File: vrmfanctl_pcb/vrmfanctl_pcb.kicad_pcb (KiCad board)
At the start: 2 copper layers, 27.9 x 22.9 mm, 6 parts, among them J1 SATA Power Male, J2 Hole, J3 Pin socket L-shape, J4 Pin socket L-shape, U1 ATtiny85-20PU

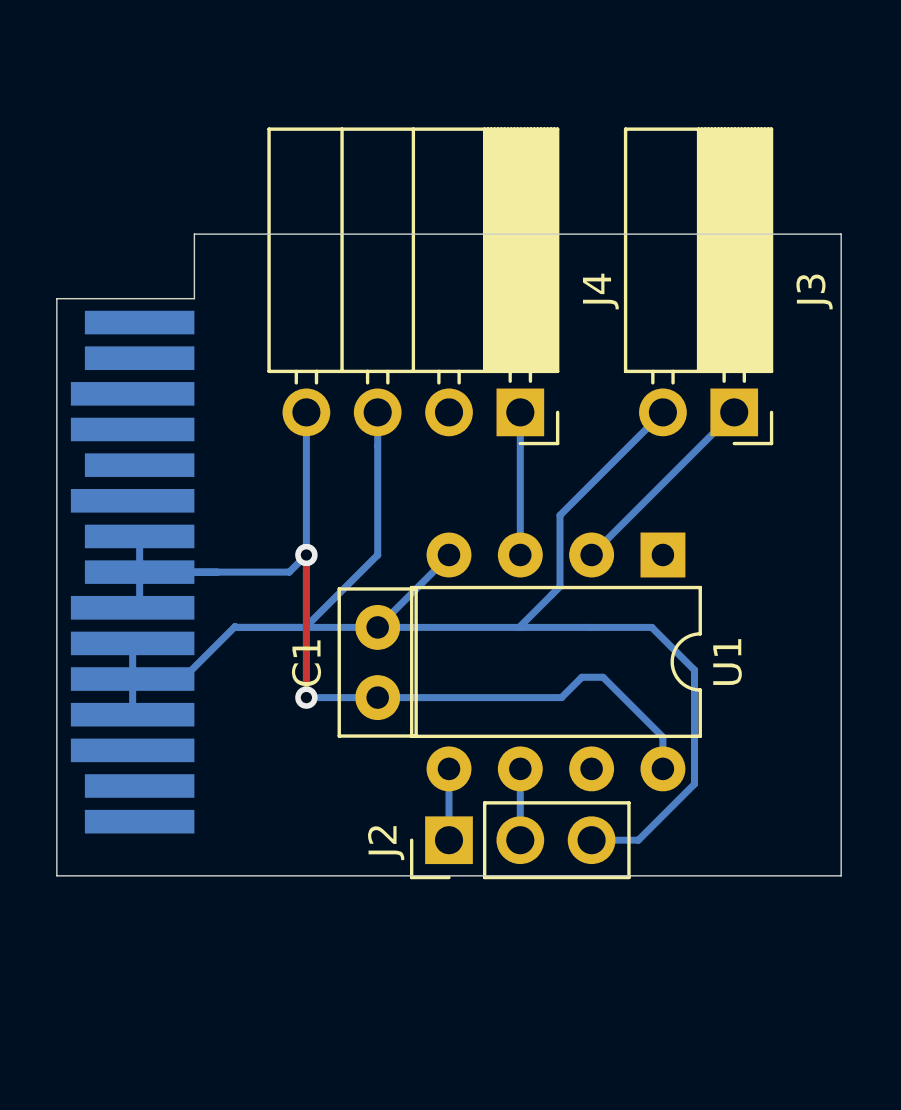
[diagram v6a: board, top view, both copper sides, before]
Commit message: add reset pin to the header
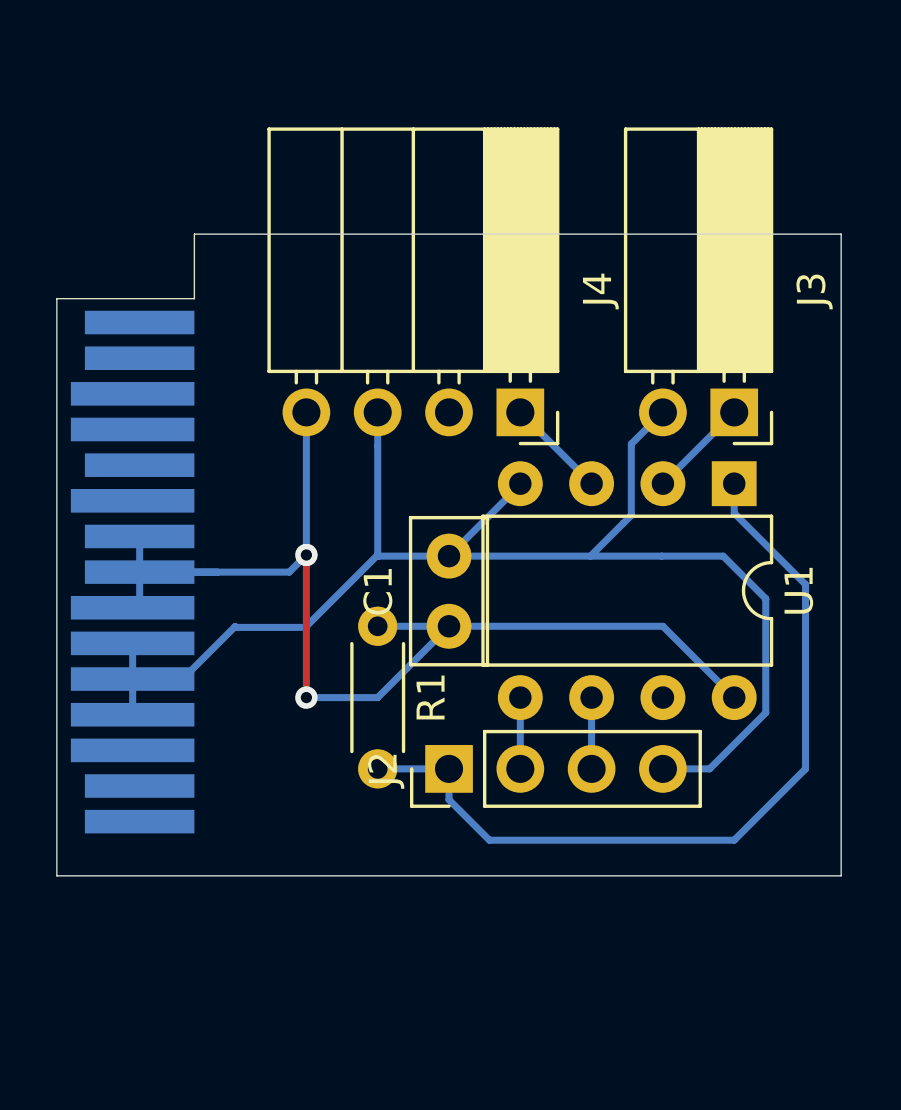
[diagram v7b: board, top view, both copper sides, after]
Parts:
- added R1: 4.7k, Resistor_THT:R_Axial_DIN0204_L3.6mm_D1.6mm_P5.08mm_Horizontal, F.Cu at (48.3, 53.3)
- J2: footprint Connector_PinHeader_2.54mm:PinHeader_1x03_P2.54mm_Vertical -> Connector_PinHeader_2.54mm:PinHeader_1x04_P2.54mm_Vertical
- moved C1 3.59 mm to (50.8, 53.3)
- moved U1 3.59 mm to (61.0, 48.3)
- moved J2 2.54 mm to (50.8, 58.4)
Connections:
- J1 pad 1: Net-(J1-Pad1) -> (no net)
- J1 pad 10: Net-(J1-Pad10) -> (no net)
- J1 pad 11: Net-(J1-Pad11) -> (no net)
- J1 pad 12: Net-(J1-Pad12) -> (no net)
- J1 pad 13: Net-(J1-Pad13) -> (no net)
- J1 pad 14: Net-(J1-Pad14) -> (no net)
- J1 pad 15: Net-(J1-Pad15) -> (no net)
- J1 pad 2: Net-(J1-Pad2) -> (no net)
- J1 pad 3: Net-(J1-Pad3) -> (no net)
- J2 pad 1: /TX -> /RESET
- J2 pad 2: /RX -> /TX
- J2 pad 3: GND -> /RX
- J4 pad 2: Net-(J4-Pad2) -> (no net)
- U1 pad 1: Net-(U1-Pad1) -> /RESET
- U1 pad 7: Net-(U1-Pad7) -> (no net)
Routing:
- net /RESET: track 0.00 -> 29.2 mm
- net GND: track 58.9 -> 52.8 mm
- net VCC: track 38.3 -> 43.2 mm
- net /D+: track 7.18 -> 3.59 mm
- net /PWM: track 5.08 -> 3.59 mm

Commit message: rewrite firmware and update pcb
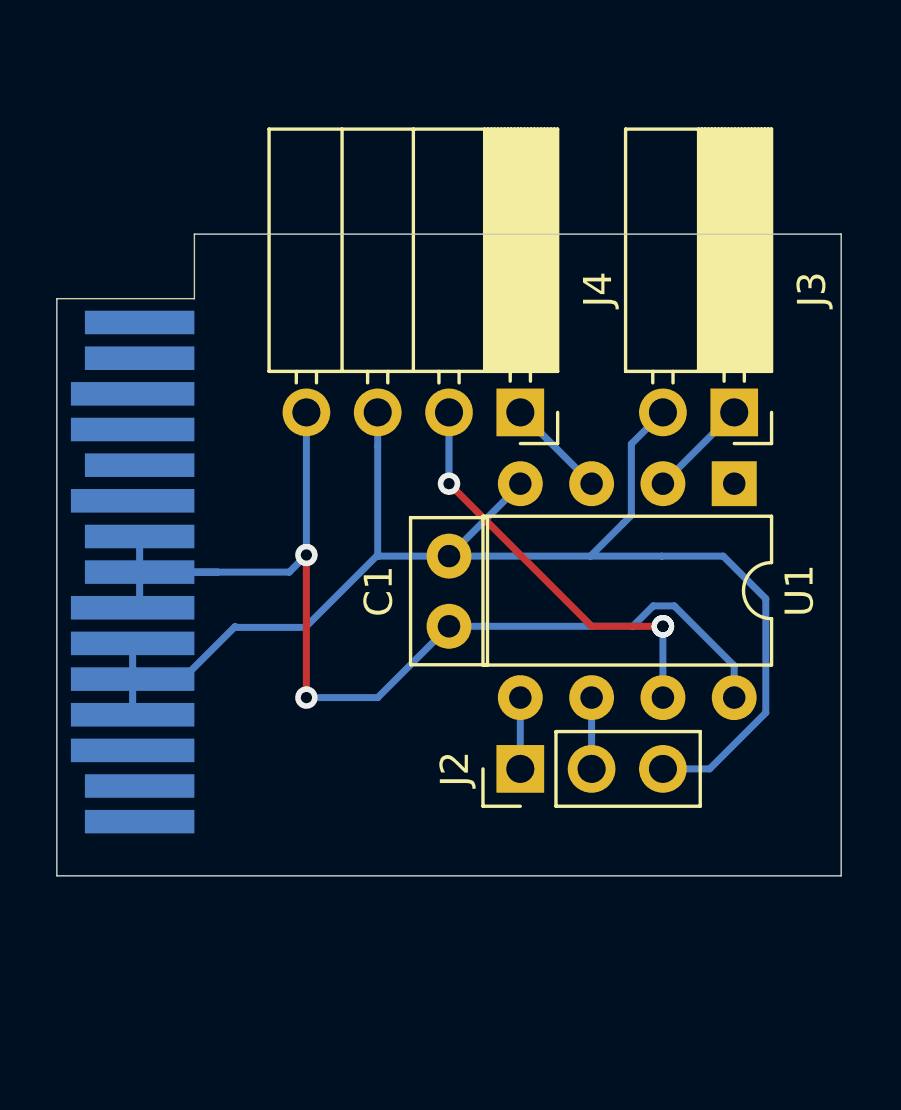
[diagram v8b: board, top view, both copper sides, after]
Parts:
- removed R1: 4.7k, Resistor_THT:R_Axial_DIN0204_L3.6mm_D1.6mm_P5.08mm_Horizontal
- J2: value Hole -> Through Hole; footprint Connector_PinHeader_2.54mm:PinHeader_1x04_P2.54mm_Vertical -> Connector_PinHeader_2.54mm:PinHeader_1x03_P2.54mm_Vertical
- moved J2 2.54 mm to (53.3, 58.4)
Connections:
- J2 pad 1: /RESET -> /TX
- J2 pad 2: /TX -> /RX
- J2 pad 3: /RX -> GND
- J4 pad 2: (no net) -> /FG
- U1 pad 1: /RESET -> (no net)
- U1 pad 7: (no net) -> /FG
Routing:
- net /RESET: track 29.2 -> 0.00 mm
- net /FG: track 0.00 -> 14.8 mm, vias 0 -> 3
- net VCC: track 43.2 -> 41.9 mm
